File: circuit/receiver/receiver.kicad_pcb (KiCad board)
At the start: 2 copper layers, 56 x 47 mm, 23 parts, among them J1 Conn_01x03_Pin, J2 Conn_01x04_Pin, J3 Conn_02x06_Top_Bottom, U4 ESP32-C3_SUPERMINI_TH

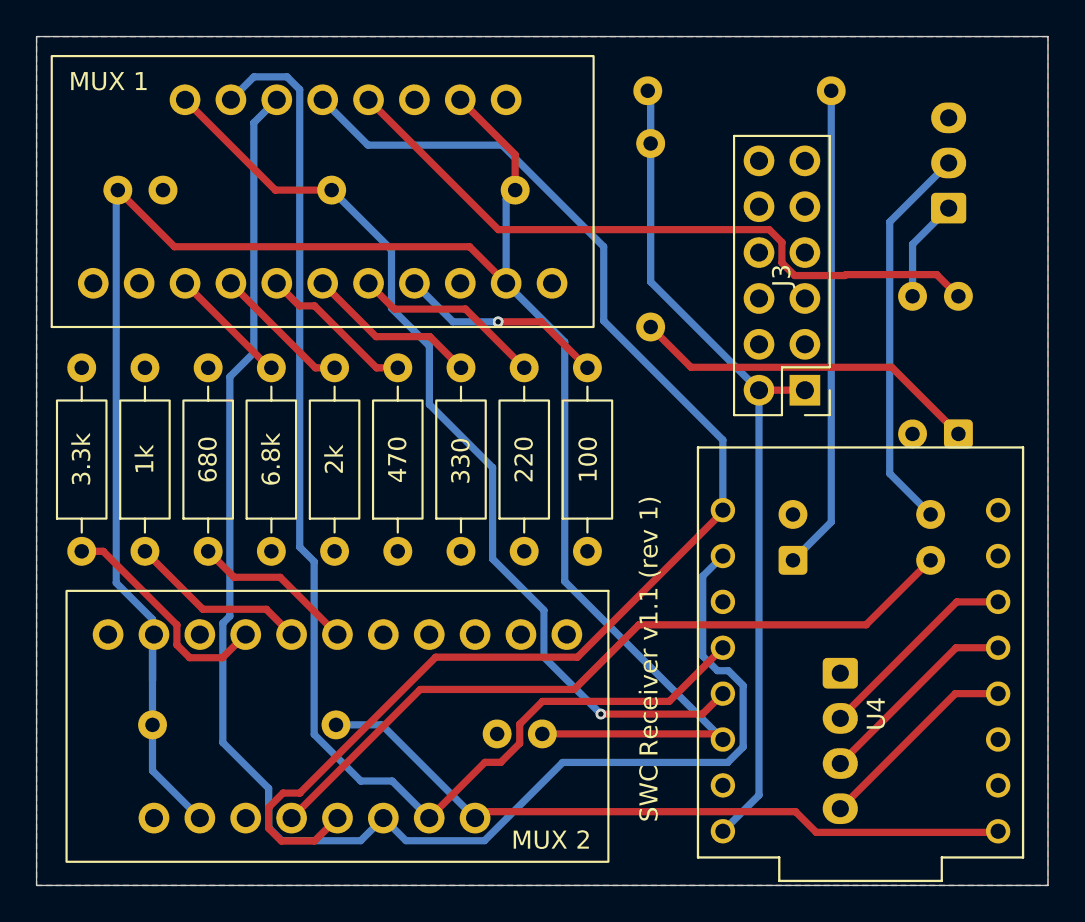
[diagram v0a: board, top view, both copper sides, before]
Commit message: fix: update circuit
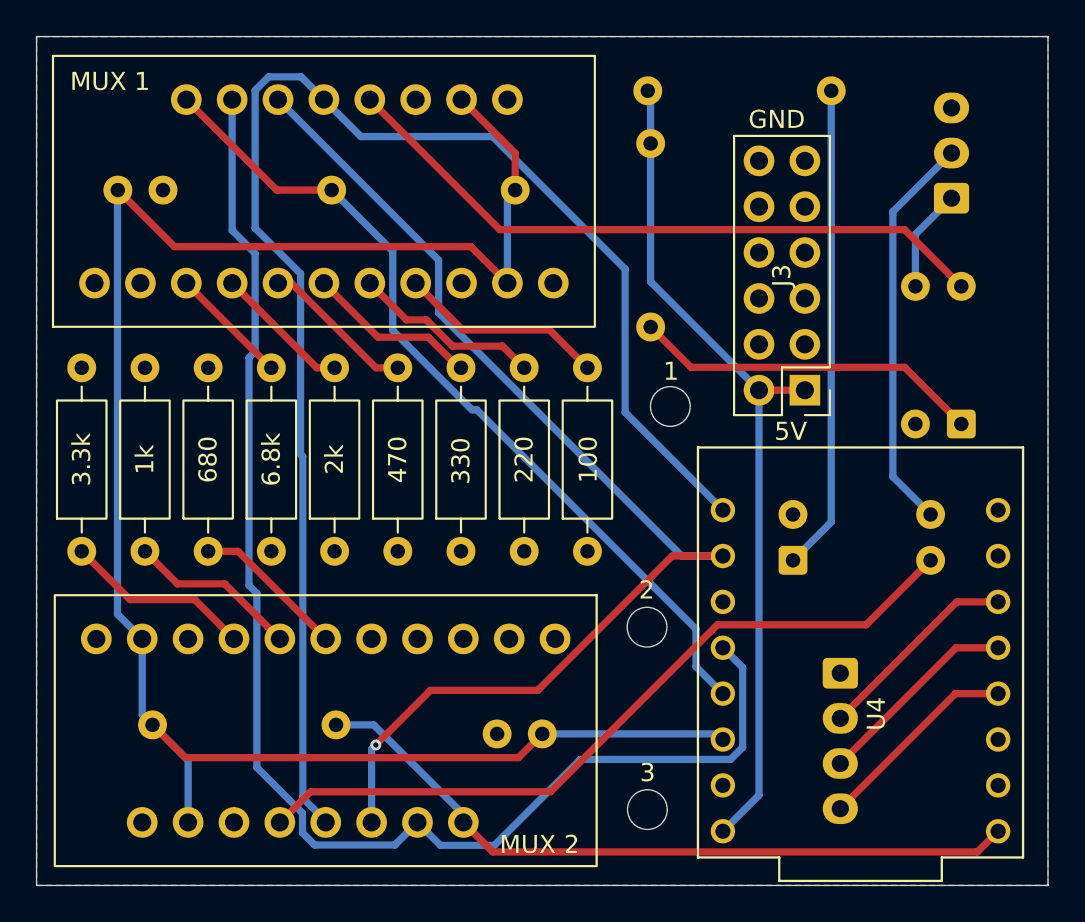
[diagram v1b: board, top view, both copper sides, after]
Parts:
- added 1: MountingHole_2.2mm_M2, MountingHole:MountingHole_2.2mm_M2, F.Cu at (166.1, 67.5)
- added 2: MountingHole_2.2mm_M2, MountingHole:MountingHole_2.2mm_M2, F.Cu at (164.8, 79.7)
- added 3: MountingHole_2.2mm_M2, MountingHole:MountingHole_2.2mm_M2, F.Cu at (164.8, 89.8)
- moved MUX 2 0.69 mm to (159.7, 80.3)
- moved J1 0.57 mm to (181.7, 56.0)
- moved photoMOS 1 0.57 mm to (182.2, 68.5)
- moved MUX 1 0.07 mm to (134.2, 60.6)
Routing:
- net Net-(U1-S1): track 84.7 -> 64.7 mm, vias 0 -> 1
- net Net-(U1-VCC): track 114.9 -> 104.9 mm
- net Net-(U1-S0): track 74.1 -> 82.9 mm
- net Net-(U1-S2): track 69.7 -> 76.4 mm
- net Net-(U2-~{E}): track 52.6 -> 47.1 mm, vias 1 -> 0
- net Net-(U1-A0): track 12.7 -> 10.4 mm
- net Net-(U1-~{E}): track 39.4 -> 40.3 mm
- net Net-(U2-A): track 37.9 -> 37.0 mm
- net Net-(U1-A): track 41.3 -> 42.0 mm
- net Net-(U1-A2): track 9.07 -> 8.52 mm
- net Net-(U1-A1): track 10.0 -> 9.48 mm
- net Net-(U2-A0): vias 1 -> 0
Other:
- board text added: "5V"
